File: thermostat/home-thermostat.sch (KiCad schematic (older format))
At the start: 52 parts, among them J1 Thermosthat, J2 Conn_01x24, J3 Conn_01x06, Q1 BC817, Q2 BC817, Q3 BSS806NL6327, U1 ESP-12F, U2 MCP7940N-xMS, U3 LM2574M-5, U4 LD1117S33TR_SOT223, U5 AT24C512, U8 MCP9844, Y1 GEY KX-327NHT 12

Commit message: Started layouting thermosthat.
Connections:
- wire segments 239 -> 240
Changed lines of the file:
@@
 Wire Wire Line
 	4750 1850 5450 1850
-Connection ~ 5450 1400
 Wire Wire Line
 	5400 2100 5650 2100
@@
 Wire Wire Line
 	4750 2350 4450 2350
-Text Label 5900 1400 2    50   ~ 0
-DTR
 Text Label 5900 2100 2    50   ~ 0
 RTS
@@
 GPIO0
 Wire Wire Line
-	6250 1850 6250 1800
-Wire Wire Line
-	6250 1800 6300 1800
-Wire Wire Line
 	6250 1250 6250 1300
 Wire Wire Line
 	6250 1300 6300 1300
-Text Label 6100 1700 0    50   ~ 0
-RXD
-Wire Wire Line
-	6100 1700 6300 1700
-Text Label 6100 1600 0    50   ~ 0
-TXD
 Wire Wire Line
 	6100 1600 6300 1600
-Wire Wire Line
-	5450 1400 6300 1400
 Wire Wire Line
 	5950 2100 5950 1500
@@
 F 3 "" H 6250 1250 50  0001 C CNN
 	1    6250 1250
-	1    0    0    -1
-$EndComp
-$Comp
-L power:GND #PWR0102
-U 1 1 5E951C47
-P 6250 1850
-F 0 "#PWR0102" H 6250 1600 50  0001 C CNN
-F 1 "GND" H 6255 1677 50  0000 C CNN
-F 2 "" H 6250 1850 50  0001 C CNN
-F 3 "" H 6250 1850 50  0001 C CNN
-	1    6250 1850
 	1    0    0    -1
 $EndComp
@@
 $EndComp
 NoConn ~ 3600 1600
+Text Label 5750 1400 2    50   ~ 0
+DTR
+$Comp
+L power:GND #PWR0102
+U 1 1 5E951C47
+P 6250 1400
+F 0 "#PWR0102" H 6250 1150 50  0001 C CNN
+F 1 "GND" H 6255 1227 50  0000 C CNN
+F 2 "" H 6250 1400 50  0001 C CNN
+F 3 "" H 6250 1400 50  0001 C CNN
+	1    6250 1400
+	0    1    1    0
+$EndComp
+Text Label 6100 1800 0    50   ~ 0
+TXD
+Text Label 6100 1600 0    50   ~ 0
+RXD
+Wire Wire Line
+	6100 1800 6300 1800
+Wire Wire Line
+	6250 1400 6300 1400
+Wire Wire Line
+	5450 1400 5850 1400
+Wire Wire Line
+	5850 1400 5850 1700
+Wire Wire Line
+	5850 1700 6300 1700
+Connection ~ 5450 1400
 $EndSCHEMATC

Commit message: Removed ESP from schematic, will switch over to NXP MKW41Z as it has better documentation, easier peripherals and support for low power thread protocol instead of WLAN to save energy in battery backed sensors. Also makes possible to use the thermostat as an access point, making the system work without routers etc.
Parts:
- removed C4: 100u, Capacitor_SMD:C_0805_2012Metric, symbol Device:C
- removed C5: 100n, Capacitor_SMD:C_0603_1608Metric, symbol Device:C
- removed J3: Conn_01x06, Connector_PinHeader_2.54mm:PinHeader_2x03_P2.54mm_Vertical_SMD, symbol Connector_Generic:Conn_01x06
- removed Q1, Q2: BC817, Package_TO_SOT_SMD:SOT-23, symbol Device:Q_NPN_BEC
- removed R1, R2, R3, R4, R5, R7, R8: 10K, Resistor_SMD:R_0603_1608Metric, symbol Device:R
- removed U1: ESP-12F, RF_Module:ESP-12E, symbol RF_Module:ESP-12F
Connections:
- net labels removed: DTR, EN, MISO, RTS, RXD, TXD, nRST
- wire segments 240 -> 179
- no-connect marks 12 -> 3
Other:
- note added: "Do we need this, the MKW41Z also has RTC?\n"
- note added: "Will we do peripherals with AVR or does MKW41Z has enough free pins?\nDo we want to try touch interface with MKW41 or AVR?"
- note removed: "ESP Bootstrapping circuit"
- note removed: "ISP programming circuit for ESP\nexternal programmer shall be used,\nMUSBUART from Waveshare"

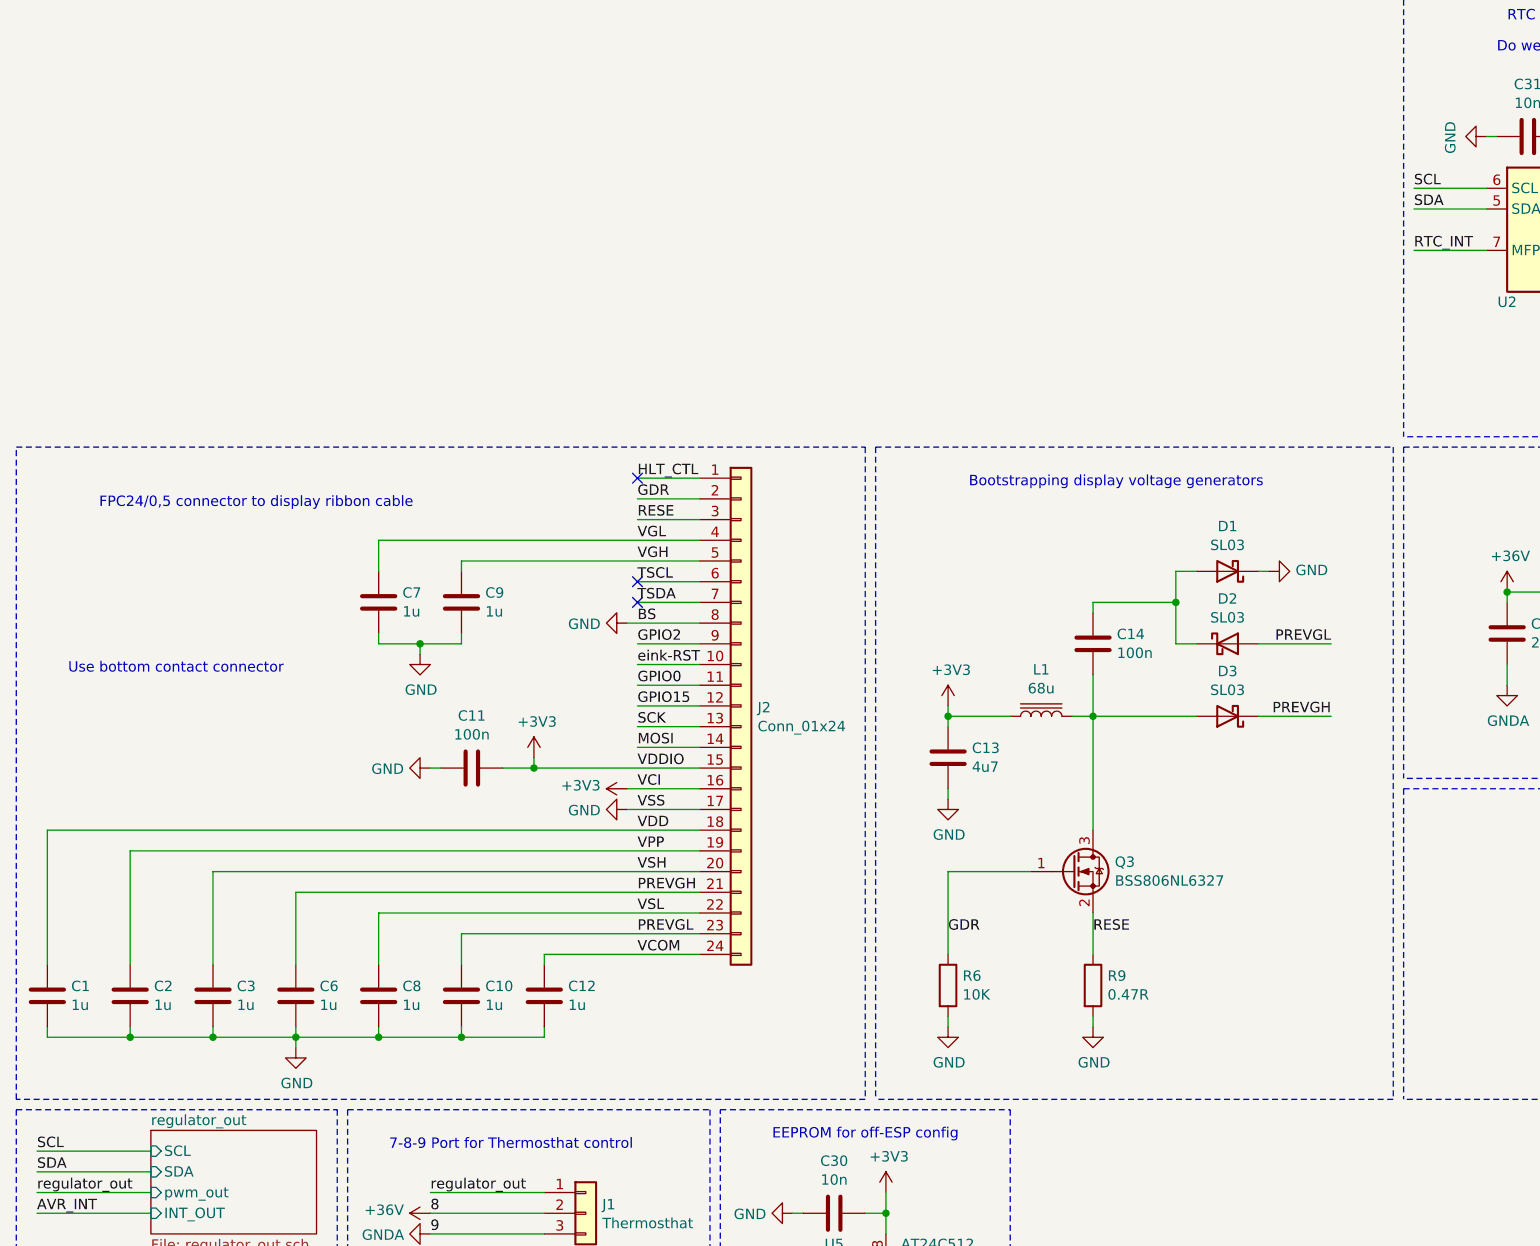
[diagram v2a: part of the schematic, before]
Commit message: Moved eINK display circuit into its own schematic to abstract control signals. Added a document about touch sensing. Touch should not be implemented on this revision.
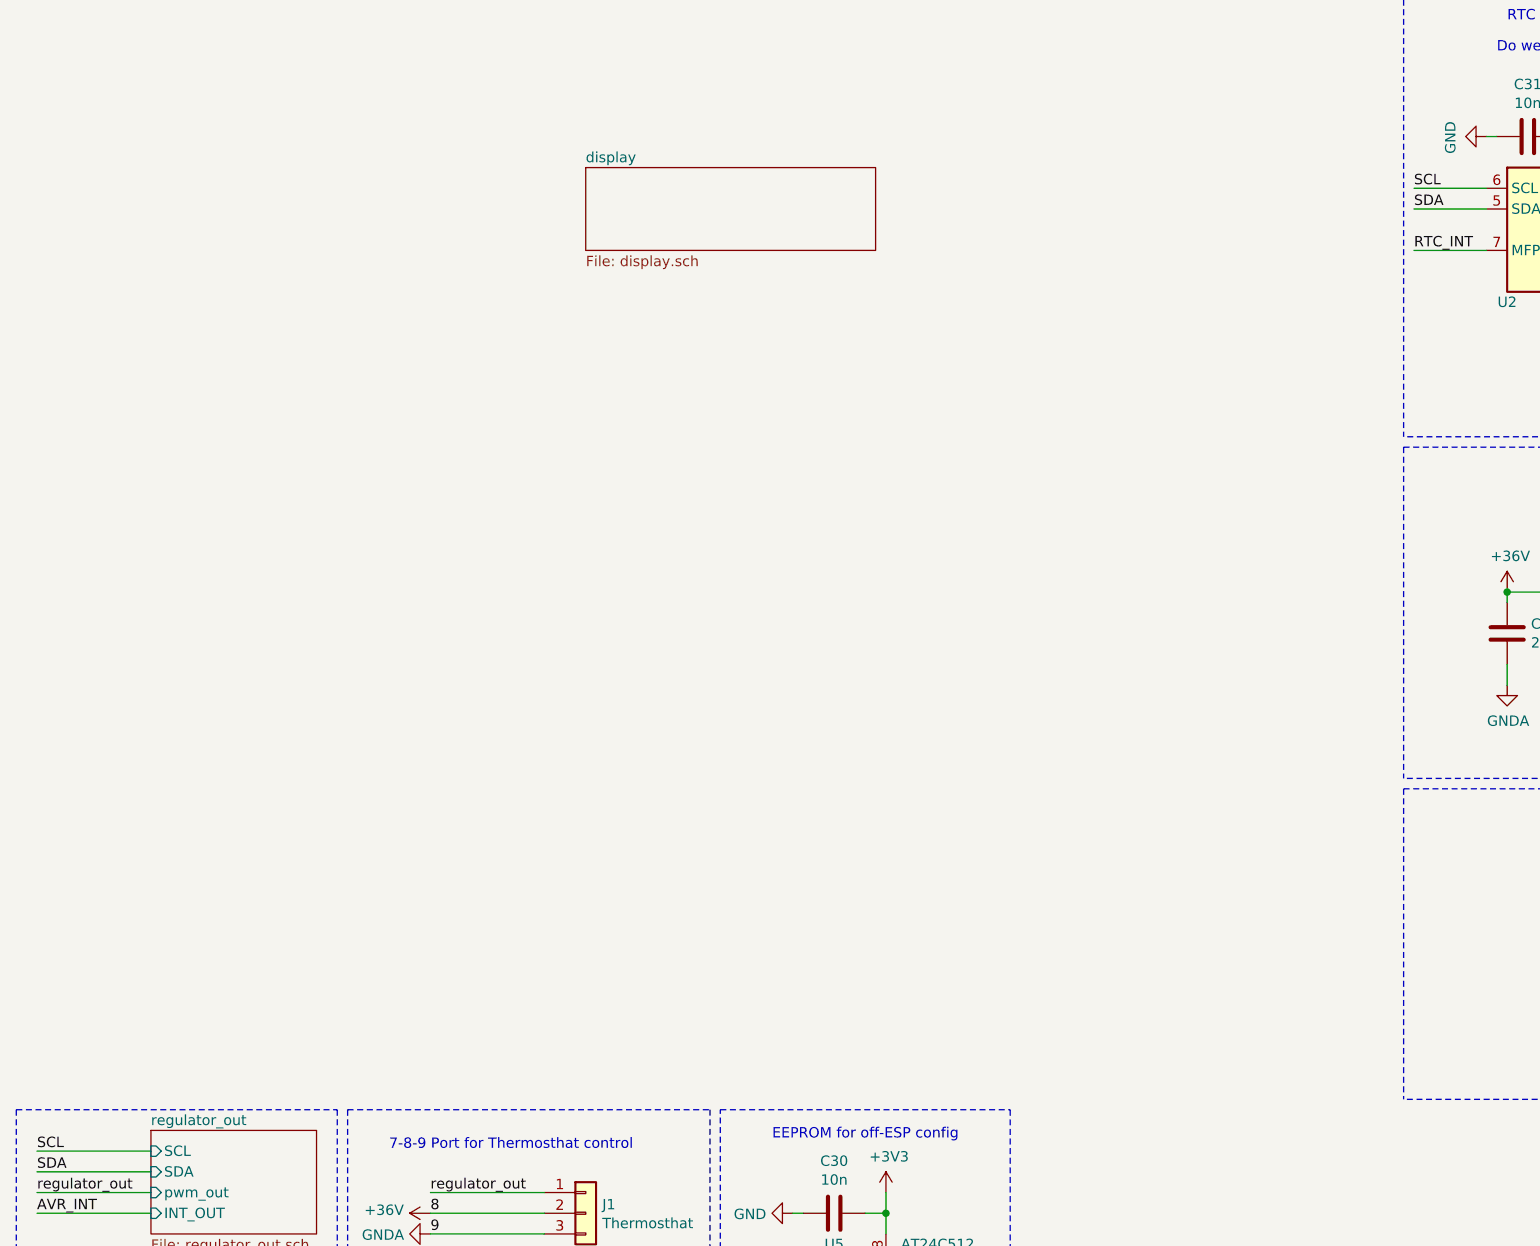
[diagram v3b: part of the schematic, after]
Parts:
- removed C1, C10, C12, C2, C3, C6, C7, C8, C9: 1u, Capacitor_SMD:C_0603_1608Metric, symbol Device:C
- removed C11, C14: 100n, Capacitor_SMD:C_0603_1608Metric, symbol Device:C
- removed C13: 4u7, Capacitor_SMD:C_0603_1608Metric, symbol Device:C
- removed D1, D2, D3: SL03, Diode_SMD:D_SMF, symbol Device:D_Schottky
- removed J2: Conn_01x24, Connector_FFC-FPC:TE_2-1734839-4_1x24-1MP_P0.5mm_Horizontal, symbol Connector_Generic:Conn_01x24
- removed L1: 68u, Inductor_SMD:L_1210_3225Metric, symbol Device:L_Core_Iron
- removed Q3: BSS806NL6327, Package_TO_SOT_SMD:SOT-23, symbol Device:Q_NMOS_GSD
- removed R6: 10K, Resistor_SMD:R_0603_1608Metric, symbol Device:R
- removed R9: 0.47R, Resistor_SMD:R_0603_1608Metric, symbol Device:R
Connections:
- no-connect marks 3 -> 0
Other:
- note removed: "Bootstrapping display voltage generators"
- note removed: "FPC24/0,5 connector to display ribbon cable"
- note removed: "Use bottom contact connector"

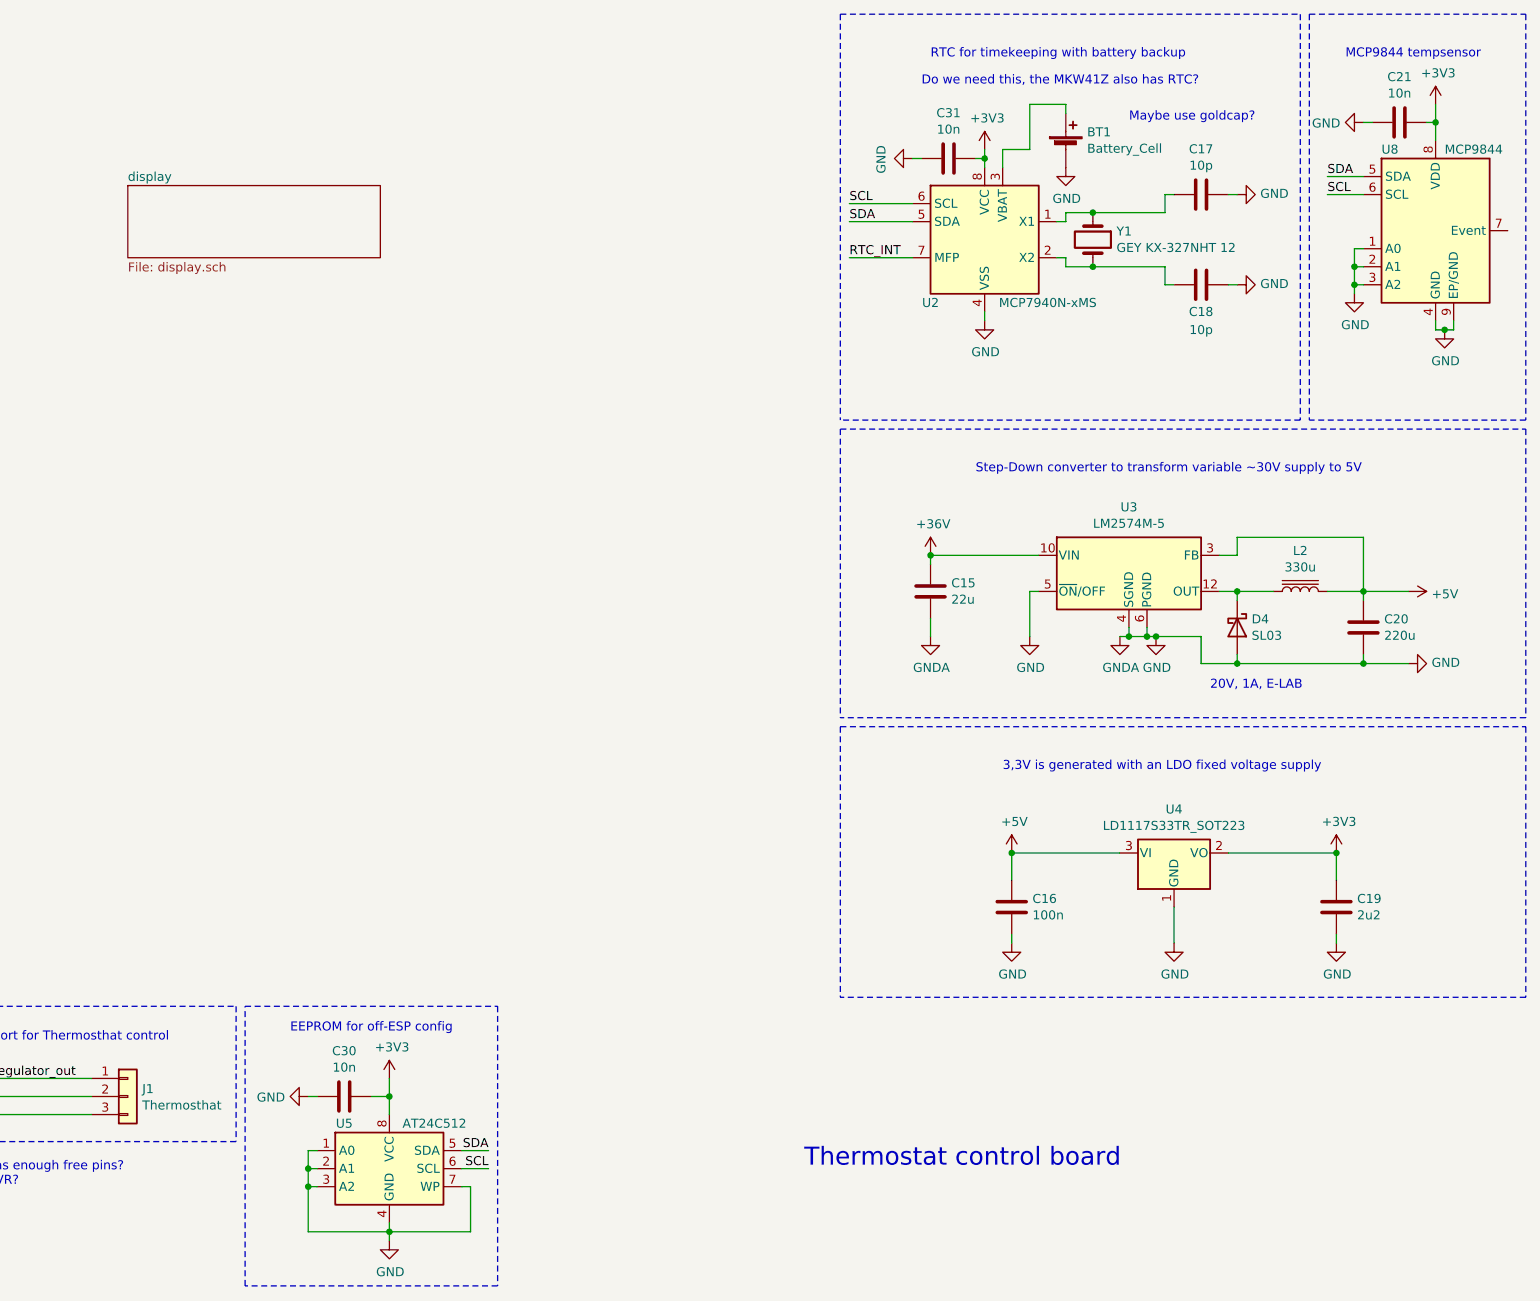
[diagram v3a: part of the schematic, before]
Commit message: Moved RTC chip and temperature sensor to separate schematic for better organisation. No interrupt from RTC chip is used as the MKW41Z has its own RTC with interrupt function and only needs the RTC chip because of its battery backup for power loss.
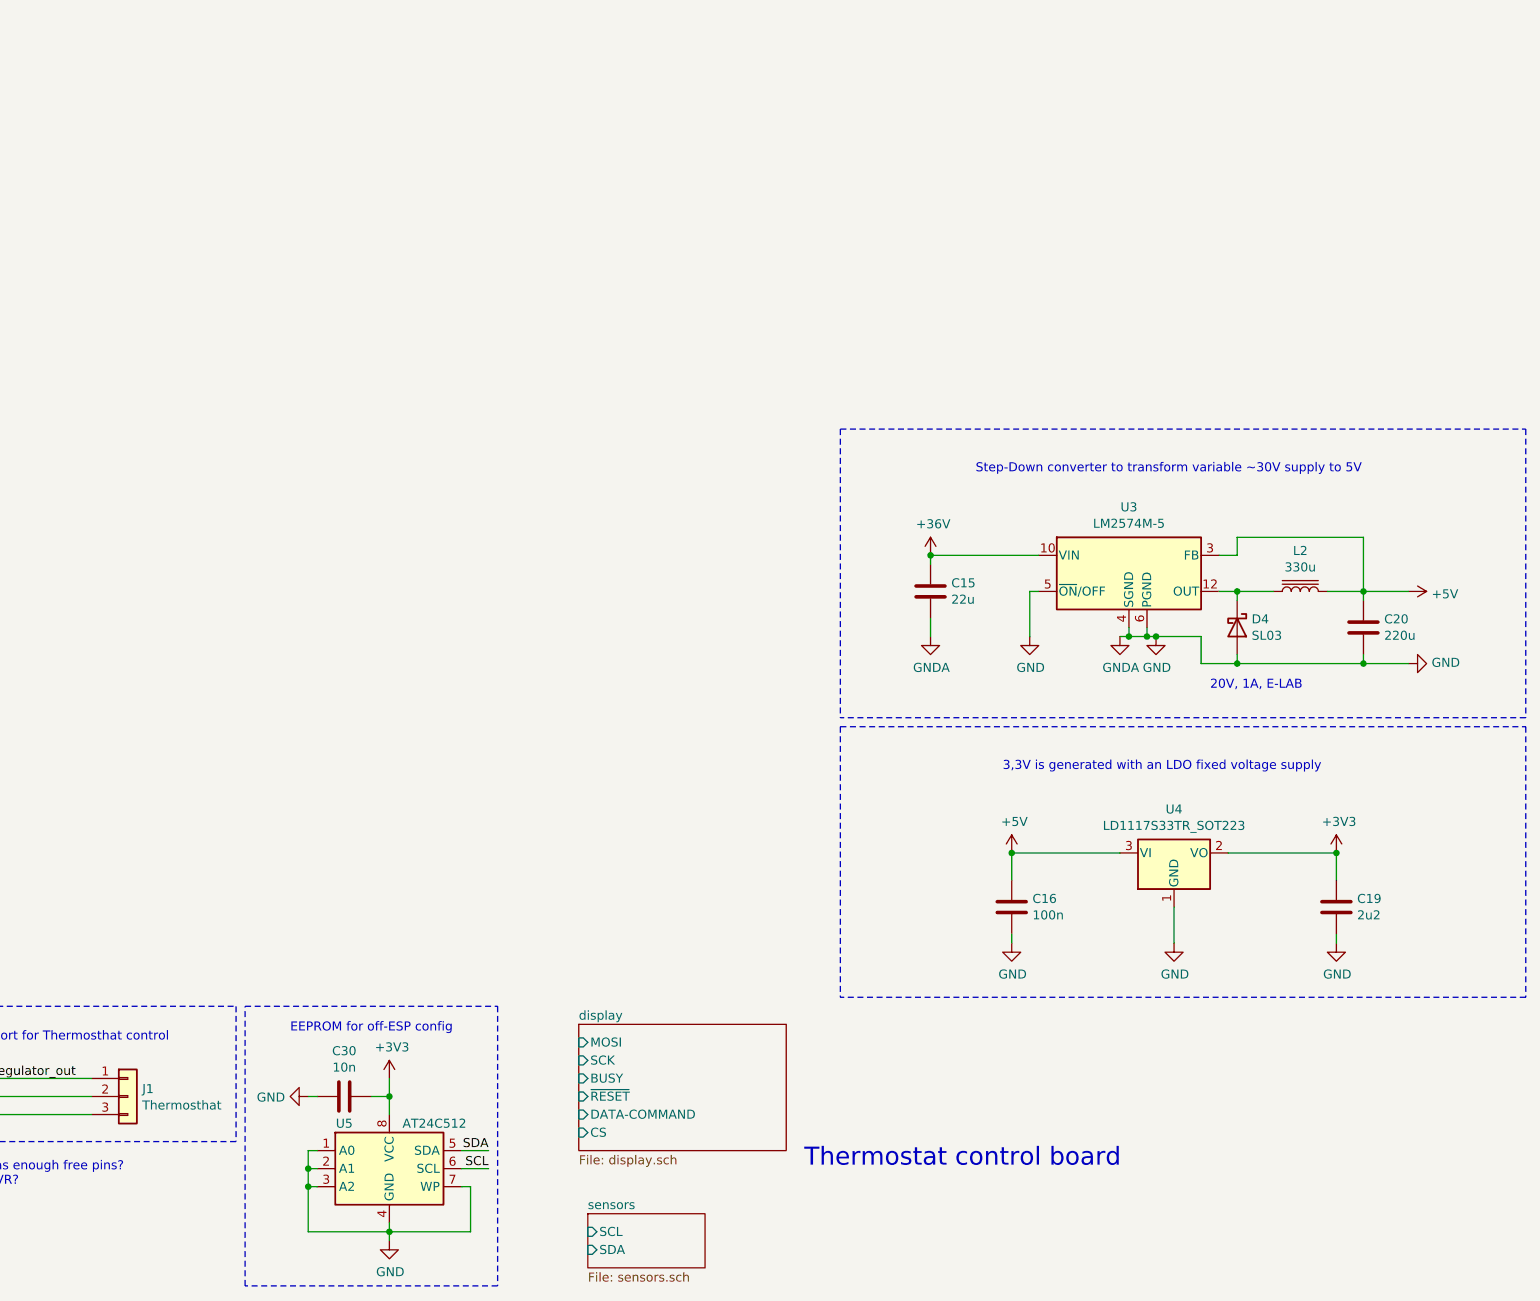
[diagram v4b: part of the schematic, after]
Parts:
- removed BT1: Battery_Cell, Battery:BatteryHolder_Keystone_3002_1x2032, symbol Device:Battery_Cell
- removed C17, C18: 10p, Capacitor_SMD:C_0603_1608Metric, symbol Device:C
- removed C21, C31: 10n, Capacitor_SMD:C_0603_1608Metric, symbol Device:C
- removed U2: MCP7940N-xMS, Package_SO:MSOP-8_3x3mm_P0.65mm, symbol Timer:MCP7940N-xMS
- removed U8: MCP9844, Package_DFN_QFN:DFN-8-1EP_3x2mm_P0.5mm_EP1.36x1.46mm, symbol Sensor_Temperature:MCP9844x-xMN
- removed Y1: GEY KX-327NHT 12, Crystal:Crystal_SMD_3215-2Pin_3.2x1.5mm, symbol Device:Crystal
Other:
- note removed: "Do we need this, the MKW41Z also has RTC?\n"
- note removed: "MCP9844 tempsensor"
- note removed: "Maybe use goldcap?"
- note removed: "RTC for timekeeping with battery backup"

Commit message: Added MKW41Z to schematic, start doing the base connections.
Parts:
- added U?: MKW41Z512VHT, Package_DFN_QFN:NXP_VQFN-48-1EP_7x7mm_P0.5mm_EP3.5x3.5mm_16xMask0.45x0.45_ThermalVias, symbol MCU_NXP_Kinetis:MKW41Z512VHT
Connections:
- net +3V3: now also U?.14 (VDD_1P8OUT), U?.15 (VDD_1P5OUT_PMCIN), U?.20 (VDD_0), U?.28 (VDDA), U?.32 (VDD_RF3), U?.35 (VDD_RF2), U?.36 (VDD_RF1), U?.44 (VDD_1), U?.9 (DCDC_CFG)
- net GND: now also U?.13 (DCDC_GND), U?.26 (VSSA), U?.49 (EPAD)
- new net RESET_b: U?.6 (PTA18)
- new net SWD_CLK: U?.5 (PTA17)
- new net SWD_DIO: U?.4 (PTA16)
- no-connect marks 0 -> 2
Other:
- moved on the sheet: C15, C16, C19, C20, C30, D4, J1, L2, U3, U4, U5
